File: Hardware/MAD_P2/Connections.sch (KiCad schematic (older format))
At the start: 14 parts, among them J1 Conn_02x05_Odd_Even, J2 Conn_02x05_Odd_Even, J3 Conn_02x05_Odd_Even, J4 Conn_02x05_Odd_Even

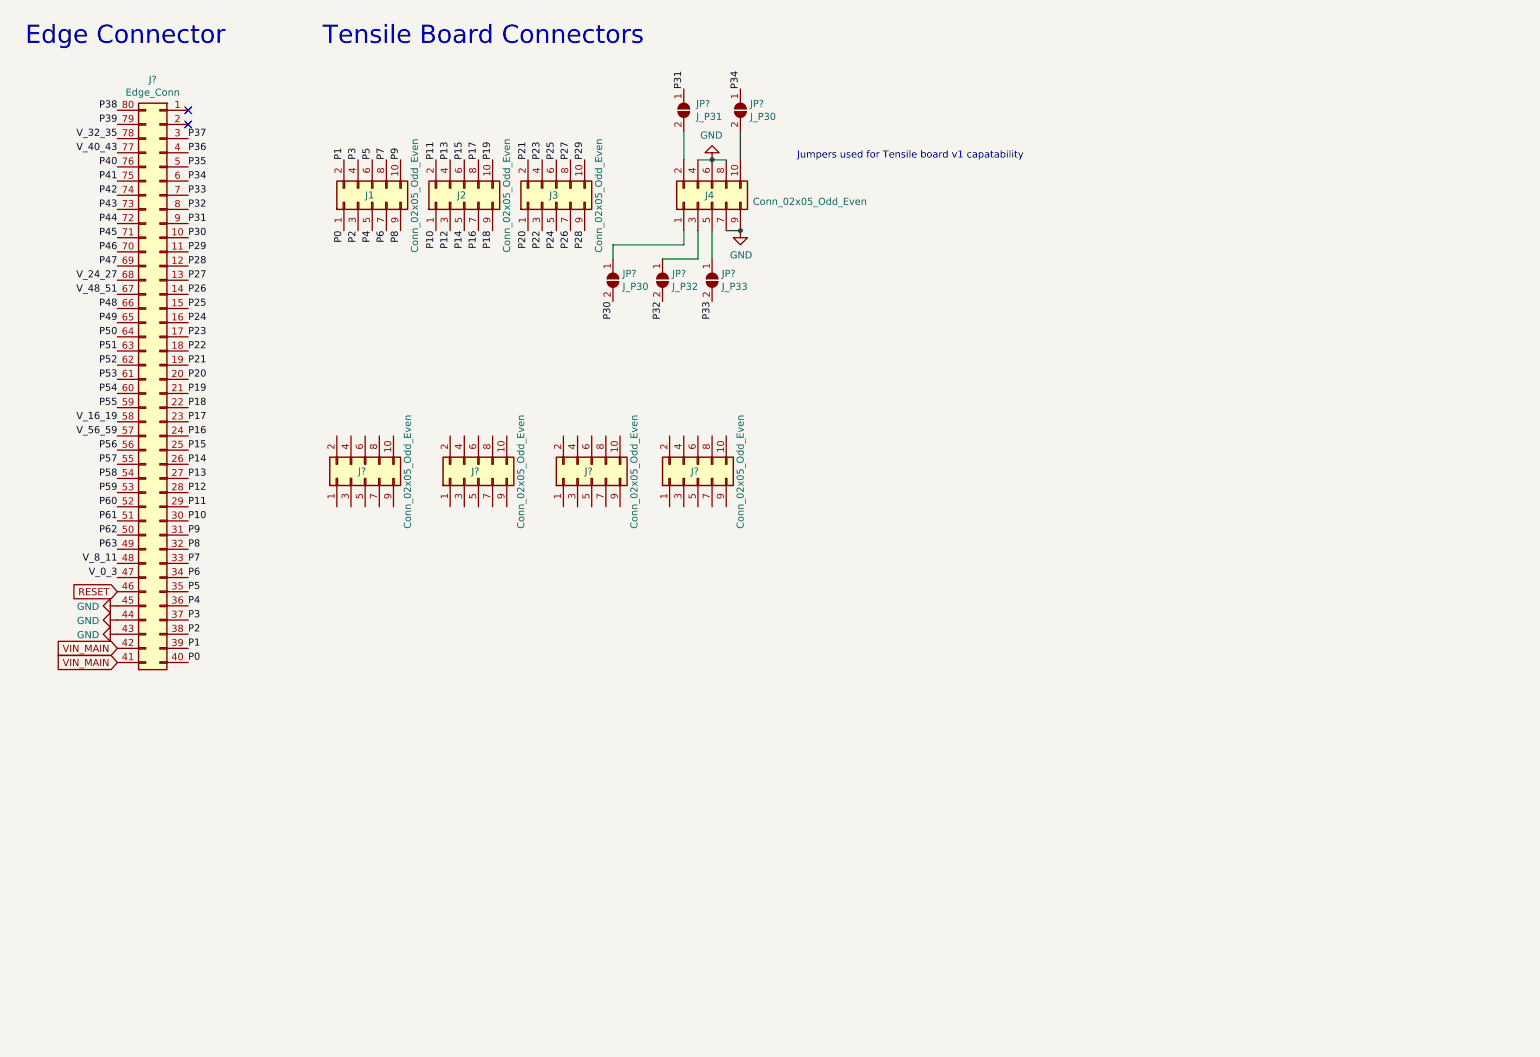
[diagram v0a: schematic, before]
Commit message: added adc
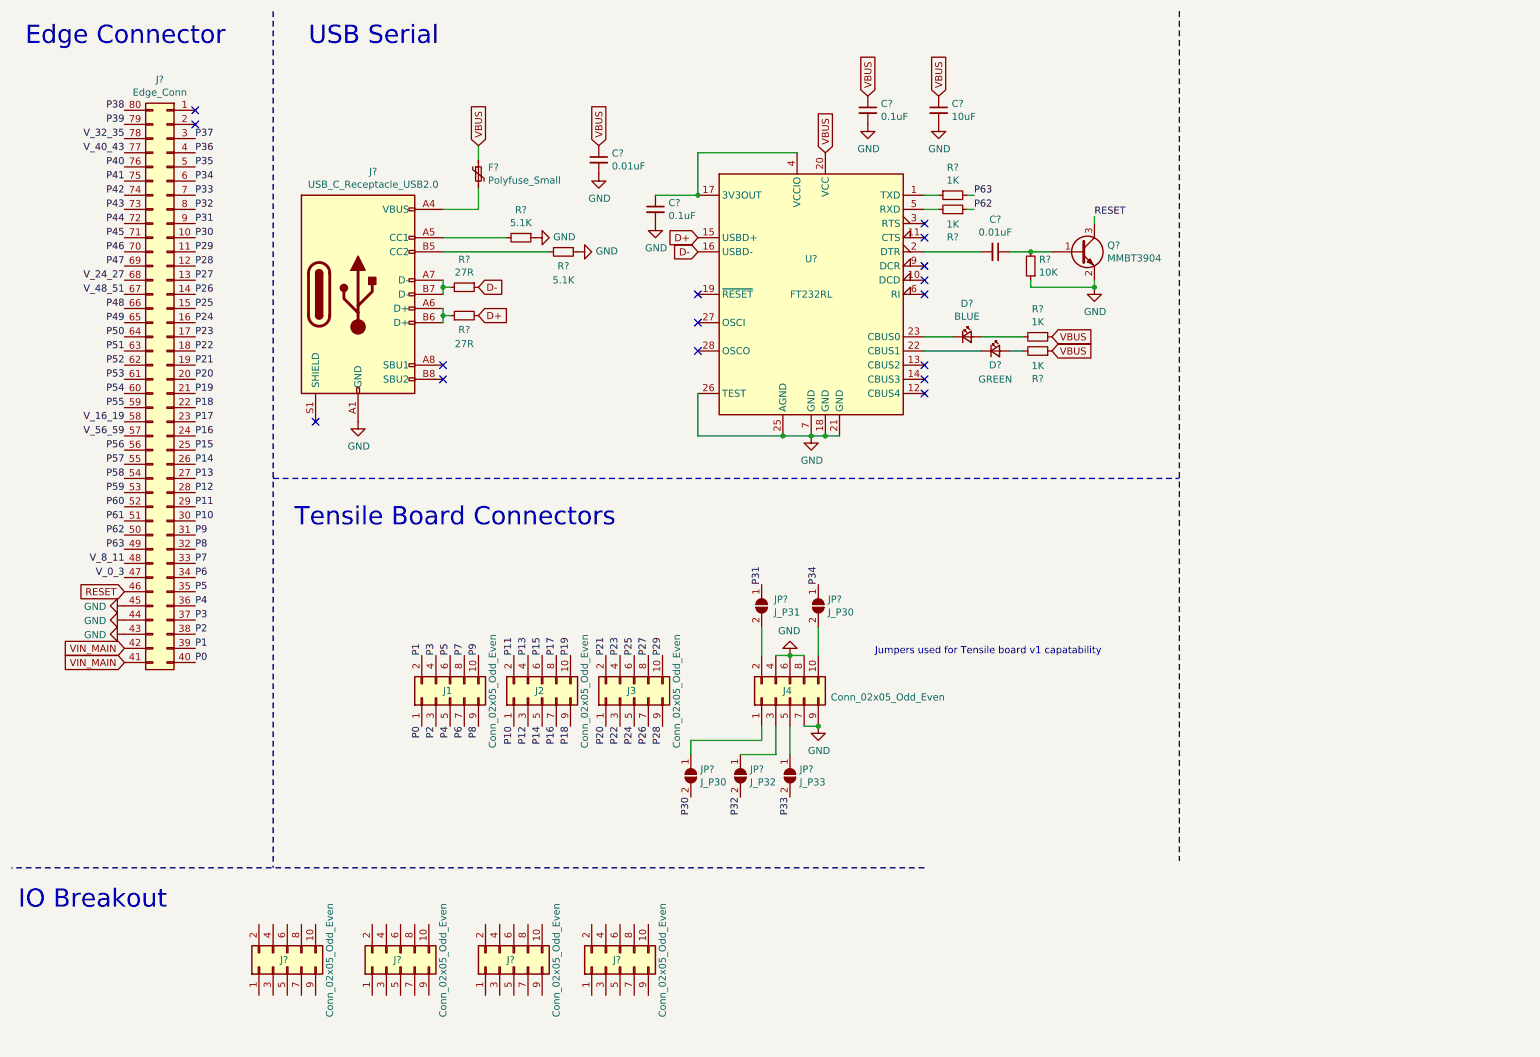
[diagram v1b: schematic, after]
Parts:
- added C? (x2): 0.1uF, symbol Device:C_Small
- added C? (x2): 0.01uF, symbol Device:C_Small
- added C?: 10uF, symbol Device:C_Small
- added D?: BLUE, symbol Device:LED_Small
- added D?: GREEN, symbol Device:LED_Small
- added F?: Polyfuse_Small, symbol Device:Polyfuse_Small
- added J?: USB_C_Receptacle_USB2.0, symbol Connector:USB_C_Receptacle_USB2.0
- added Q?: MMBT3904, Package_TO_SOT_SMD:SOT-23, symbol Transistor_BJT:MMBT3904
- added R? (x2): 5.1K, symbol Device:R_Small
- added R? (x4): 1K, symbol Device:R_Small
- added R?: 10K, symbol Device:R_Small
- added R? (x2): 27R, symbol Device:R_Small
- added U?: FT232RL, Package_SO:SSOP-28_5.3x10.2mm_P0.65mm, symbol Interface_USB:FT232RL
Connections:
- net GND: now also C?.2, C?.2, C?.2, C?.2, J?.A1 (GND), J?.A12 (GND), J?.B1 (GND), J?.B12 (GND), Q?.2 (E), R?.1, R?.1, R?.1, U?.18 (GND), U?.21 (GND), U?.25 (AGND), U?.26 (TEST), U?.7 (GND)
- net P62: now also R?.1
- net P63: now also R?.2
- net RESET: now also Q?.3 (C)
- new net: F?.2, J?.A4 (VBUS), J?.A9 (VBUS), J?.B4 (VBUS), J?.B9 (VBUS)
- new net: J?.A5 (CC1), R?.2
- new net: J?.A6 (D+), J?.B6 (D+), R?.1
- new net: J?.A7 (D-), J?.B7 (D-), R?.2
- new net: J?.B5 (CC2), R?.2
- new net: R?.1, U?.1 (TXD)
- new net: C?.1, U?.17 (3V3OUT), U?.4 (VCCIO)
- new net: C?.2, U?.2 (DTR)
- new net: D?.1 (K), U?.22 (CBUS1)
- new net: D?.1 (K), U?.23 (CBUS0)
- new net: R?.2, U?.5 (RXD)
- new net: D?.2 (A), R?.2 (x2)
- new net: C?.1, Q?.1 (B), R?.2
- new net D+: R?.2, U?.15 (USBD+)
- new net D-: R?.1, U?.16 (USBD-)
- new net VBUS: C?.1, C?.1, C?.1, F?.1, R?.1, R?.1, U?.20 (VCC)
- no-connect marks 2 -> 16
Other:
- note added: "IO Breakout"
- note added: "USB Serial"
- moved on the sheet: J1, J2, J3, J4, J?, JP?

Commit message: began pcb layout
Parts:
- added J15: Conn_ADC1, Connector_IDC:IDC-Header_2x05_P2.54mm_Vertical, symbol Connector_Generic:Conn_02x05_Odd_Even
- added J16: Conn_DAC, Connector_IDC:IDC-Header_2x05_P2.54mm_Vertical, symbol Connector_Generic:Conn_02x05_Odd_Even
- added J17: Conn_ADC2, Connector_IDC:IDC-Header_2x05_P2.54mm_Vertical, symbol Connector_Generic:Conn_02x05_Odd_Even
- C103, C104, C105, C106, C107: renamed from C?; footprint (none) -> Capacitor_SMD:C_0603_1608Metric
- D12, D9: renamed from D?; footprint (none) -> LED_SMD:LED_0603_1608Metric
- F4: renamed from F?; footprint (none) -> Fuse:Fuse_0603_1608Metric
- J10, J11, J7, J9: renamed from J?; footprint (none) -> Connector_IDC:IDC-Header_2x05_P2.54mm_Vertical
- J13: renamed from J3; footprint (none) -> Connector_IDC:IDC-Header_2x05_P2.54mm_Vertical
- J14: renamed from J4; footprint (none) -> Connector_IDC:IDC-Header_2x05_P2.54mm_Vertical
- J21: renamed from J1; footprint (none) -> Connector_IDC:IDC-Header_2x05_P2.54mm_Vertical
- J22: renamed from J2; footprint (none) -> Connector_IDC:IDC-Header_2x05_P2.54mm_Vertical
- J6: renamed from J?; footprint (none) -> MAD_P2:P2_Edge_Conn
- J8: renamed from J?; footprint (none) -> Connector_USB:USB_C_Receptacle_Palconn_UTC16-G
- JP13, JP14, JP15, JP16, JP17: renamed from JP?; footprint (none) -> Jumper:SolderJumper-2_P1.3mm_Open_Pad1.0x1.5mm
- R14, R15, R16, R17, R18, R19, R20, R21, R22: renamed from R?; footprint (none) -> Resistor_SMD:R_0603_1608Metric
- gave numbers to parts that had none: 2
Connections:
- net GND: now also J11.10 (Pin_10), J11.7 (Pin_7), J11.8 (Pin_8), J11.9 (Pin_9), J15.9 (Pin_9), J16.4 (Pin_4), J16.6 (Pin_6), J16.7 (Pin_7), J16.8 (Pin_8), J16.9 (Pin_9), J17.9 (Pin_9)
- net P34: now also J7.1 (Pin_1)
- net P35: now also J7.2 (Pin_2)
- net P36: now also J7.3 (Pin_3)
- net P37: now also J7.4 (Pin_4)
- net P38: now also J7.5 (Pin_5)
- net P39: now also J7.6 (Pin_6)
- net P40: now also J7.7 (Pin_7)
- net P41: now also J7.8 (Pin_8)
- net P42: now also J7.9 (Pin_9)
- net P43: now also J7.10 (Pin_10)
- net P44: now also J9.1 (Pin_1)
- net P45: now also J9.2 (Pin_2)
- net P46: now also J9.3 (Pin_3)
- net P47: now also J9.4 (Pin_4)
- net P48: now also J9.5 (Pin_5)
- net P49: now also J9.6 (Pin_6)
- net P50: now also J9.7 (Pin_7)
- net P51: now also J9.8 (Pin_8)
- net P52: now also J9.9 (Pin_9)
- net P53: now also J9.10 (Pin_10)
- net P54: now also J10.1 (Pin_1)
- net P55: now also J10.2 (Pin_2)
- net P56: now also J10.3 (Pin_3)
- net P57: now also J10.4 (Pin_4)
- net P58: now also J10.5 (Pin_5)
- net P59: now also J10.6 (Pin_6)
- net P60: now also J10.7 (Pin_7)
- net P61: now also J10.8 (Pin_8)
- net P62: now also J10.9 (Pin_9)
- net P63: now also J10.10 (Pin_10)
- net VIN_MAIN: now also J11.6 (Pin_6)
- net V_0_3: now also J11.2 (Pin_2)
- net V_16_19: now also J11.3 (Pin_3)
- net V_32_35: now also J11.4 (Pin_4)
- net V_48_51: now also J11.5 (Pin_5)
- net P64: now reaches J11.1 (Pin_1)
- new net 3.3V_ADC: J15.10 (Pin_10), J16.1 (Pin_1), J16.3 (Pin_3), J17.10 (Pin_10)
- new net A01: J16.2 (Pin_2)
- new net A02: J16.5 (Pin_5)
- new net A03: J16.10 (Pin_10)
- new net IN1N: J15.2 (Pin_2)
- new net IN1P: J15.1 (Pin_1)
- new net IN2N: J15.4 (Pin_4)
- new net IN2P: J15.3 (Pin_3)
- new net IN3N: J15.6 (Pin_6)
- new net IN3P: J15.5 (Pin_5)
- new net IN4N: J15.8 (Pin_8)
- new net IN4P: J15.7 (Pin_7)
- new net IN5N: J17.2 (Pin_2)
- new net IN5P: J17.1 (Pin_1)
- new net IN6N: J17.4 (Pin_4)
- new net IN6P: J17.3 (Pin_3)
- new net IN7N: J17.6 (Pin_6)
- new net IN7P: J17.5 (Pin_5)
- new net IN8N: J17.8 (Pin_8)
- new net IN8P: J17.7 (Pin_7)
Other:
- note added: "ADC"
- note added: "DAC"

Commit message: finished board layout
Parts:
- added J18: P3, Connector_PinSocket_2.54mm:PinSocket_1x08_P2.54mm_Vertical, symbol Connector_Generic:Conn_01x08
- added J19: P4, Connector_PinSocket_2.54mm:PinSocket_1x08_P2.54mm_Vertical, symbol Connector_Generic:Conn_01x08
- added J20: P2, Connector_PinSocket_2.54mm:PinSocket_1x08_P2.54mm_Vertical, symbol Connector_Generic:Conn_01x08
- added J23: Conn_02x03_Odd_Even, Connector_PinSocket_2.54mm:PinSocket_2x03_P2.54mm_Vertical, symbol Connector_Generic:Conn_02x03_Odd_Even
- added J24: P5, Connector_PinSocket_2.54mm:PinSocket_1x10_P2.54mm_Vertical, symbol Connector_Generic:Conn_01x10
- added J25: P6, Connector_PinSocket_2.54mm:PinSocket_1x08_P2.54mm_Vertical, symbol Connector_Generic:Conn_01x08
- added J26: P7, Connector_PinSocket_2.54mm:PinSocket_1x08_P2.54mm_Vertical, symbol Connector_Generic:Conn_01x08
- added R1: 10K, Resistor_SMD:R_0603_1608Metric, symbol Device:R_Small
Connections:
- net GND: now also J20.6 (Pin_6), J20.7 (Pin_7), J23.5 (Pin_5), J24.4 (Pin_4)
- net P51: now also J23.4 (Pin_4)
- net P52: now also J23.3 (Pin_3)
- net P53: now also J23.2 (Pin_2)
- net P54: now also J24.9 (Pin_9)
- net P55: now also J24.8 (Pin_8)
- net P56: now also J26.8 (Pin_8)
- net P57: now also J26.7 (Pin_7)
- net RESET: now also J20.3 (Pin_3), J23.6 (Pin_6)
- net VIN_MAIN: now also J20.8 (Pin_8)
- net IN1N renamed A1-
- net IN1P renamed A1+
- net IN2N renamed A2-
- net IN2P renamed A2+
- net IN3N renamed A3-
- net IN3P renamed A3+
- net IN4N renamed A4-
- net IN4P renamed A4+
- net IN5N renamed A5-
- net IN5P renamed A5+
- net IN6N renamed A6-
- net IN6P renamed A6+
- net IN7N renamed A7-
- net IN7P renamed A7+
- net IN8N renamed A8-
- net IN8P renamed A8+
- new net: J24.10 (Pin_10), R1.2
- new net 3.3V_MAIN: J20.2 (Pin_2), J20.4 (Pin_4)
- new net 5V_MAIN: J20.5 (Pin_5), J23.1 (Pin_1), R1.1
- no-connect marks 16 -> 53

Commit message: added lcsc part numbers to bom
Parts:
- C103, C107: LCSC (none) -> C1634; TYPE (none) -> BASIC
- C104, C105: LCSC (none) -> C14663; TYPE (none) -> BASIC
- C106: footprint Capacitor_SMD:C_0603_1608Metric -> Capacitor_SMD:C_0805_2012Metric; LCSC (none) -> C15850; TYPE (none) -> EXT
- D12: LCSC (none) -> C72043; TYPE (none) -> BASIC
- D9: LCSC (none) -> C72041; TYPE (none) -> BASIC
- F4: footprint Fuse:Fuse_0603_1608Metric -> Fuse:Fuse_0805_2012Metric; LCSC (none) -> C261942; TYPE (none) -> EXT
- J10, J11, J13, J14, J15, J16, J17, J21, J22, J23, J7, J9: LCSC (none) -> C93705; TYPE (none) -> EXT
- J18, J19, J20, J24, J25, J26, J6, JP13, JP14, JP15, JP16, JP17: TYPE (none) -> NA
- Q1: LCSC (none) -> C20526; TYPE (none) -> BASIC
- R1, R20: LCSC (none) -> C25804; TYPE (none) -> BASIC
- R14, R15: LCSC (none) -> C22966; TYPE (none) -> BASIC
- R16, R17: LCSC (none) -> C23186; TYPE (none) -> BASIC
- R18, R19, R21, R22: LCSC (none) -> C21190; TYPE (none) -> BASIC
- U27: LCSC (none) -> C8690; TYPE (none) -> BASIC
